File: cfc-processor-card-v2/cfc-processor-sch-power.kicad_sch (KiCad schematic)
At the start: 89 parts, among them Q1 DMP2240UDM, Q2 PMV45EN, Q3 DMP3050LVT-7, Q4 DMP3050LVT-7, Q5 PMV45EN, U1 MAX7310ATE+, U2 MIC842LYC5, U3 MIC842LYC5, U4 TS5A21366, U5 MAX4211FETE, U6 TPS62112

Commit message: Update
Updated OPD to align with proto card. Made changes from DR with Greenberg. Moved around polygon pours, led indicators, silkscreen issue date, etc. Ready for fab.
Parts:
- removed TP16, TP17, TP19: TEST-POINT, oresat-misc:TestPoint-0.75mm-th, symbol oresat-misc:Test-Point-0.75mm-th
- Q2, Q5: value PMV45EN -> DMN2050LQ-7; DPN 1727-2307-1-ND -> 31-DMN2050LQ-7CT-ND; MFR Nexperia -> Diodes Incorporated; MPN PMV45EN2R -> DMN2050LQ-7
- Q3, Q4: value DMP3050LVT-7 -> DMPH2040UVTQ-7; DPN DMP3050LVT-7DICT-ND -> 31-DMPH2040UVTQ-7CT-ND; MFR Diodes Inc -> Diodes Incorporated; MPN DMP3050LVT-7 -> DMPH2040UVTQ-7
- R1: value 10 -> 100; DPN RMCF0603FT10R0CT-ND -> RMCF0603FT100RCT-ND; MPN RMCF0603FT10R0 -> RMCF0603FT100R
- R11, R13, R3: value 100 -> 1k; DIS DigiKey -> Digi-Key; DPN RMCF0603FT100RCT-ND -> 1276-4275-1-ND; MFR Stackpole Electronics Inc -> Samsung; MPN RMCF0603FT100R -> RC1005F6653CS
- R24: value 10k -> 1k; DIS DigiKey -> Digi-Key; DPN RMCF0603FT10K0CT-ND -> 1276-4275-1-ND; MFR Stackpole Electronics Inc -> Samsung; MPN RMCF0603FT10K0 -> RC1005F6653CS
- R28: value 2.7k -> 4.7k; DPN RMCF0603FT2K70CT-ND -> RMCF0603FT4K70CT-ND; MPN RMCF0603FT2K70 -> RMCF0603FT4K70
- R39, R41: value 2.7k -> 10k; DPN RMCF0603FT2K70CT-ND -> RMCF0603FT10K0CT-ND; MPN RMCF0603FT2K70 -> RMCF0603FT10K0

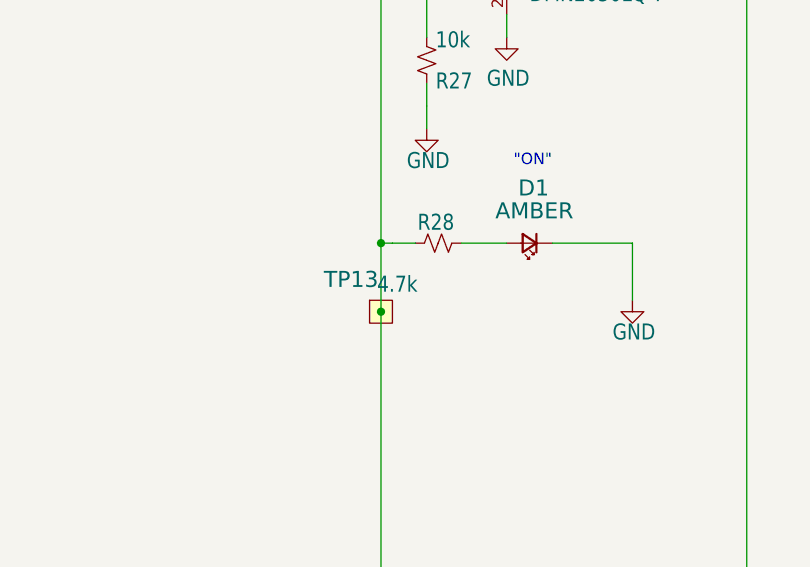
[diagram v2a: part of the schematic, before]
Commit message: Updated OPD on sensor card
updated OPD on sensor card to match protocard. Finished placement on PCB.
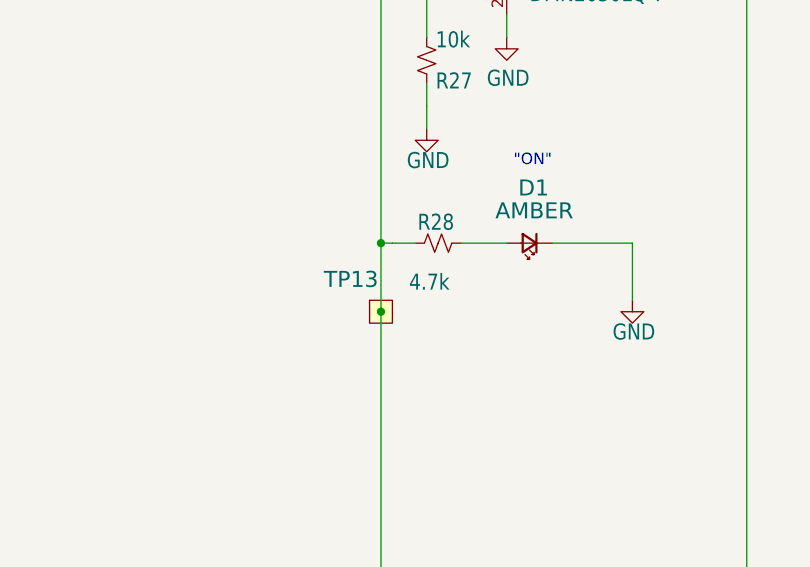
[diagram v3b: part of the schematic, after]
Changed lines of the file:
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@@
 		)
 		(property "Value" "4.7k"
-			(at 209.804 89.8906 90)
+			(at 213.36 89.662 90)
 			(show_name no)
 			(do_not_autoplace no)

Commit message: Update
Updated BOM, couple of fixes on OPD. Minor routing and layout changes. Removed logic gates from sensor card.
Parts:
- C1, C2, C6, C7, C9: DIS DigiKey -> Digikey; DPN 587-3473-1-ND -> 490-10675-2-ND; MFR Taiyo Yuden -> Murata Electronics; MPN TMK107BJ105KAHT -> GCM21BR71H105KA03L
- C10: DPN 490-GCM32EC71E226KE36KCT-ND -> 587-5949-1-ND; MFR Murata Electronics -> Taiyo Yuden; MPN GCM32EC71E226KE36K -> TMK325B7226KMHP
- C3, C4: DPN 587-3472-1-ND -> 399-6856-1-ND; MFR Taiyo Yuden -> KEMET; MPN TMK107BJ104KAHT -> C0603C104K5RACAUTO
- C5, C8: DPN 490-GRT21BC71E106KE13LCT-ND -> 490-GRT21BC71E106KE13KCT-ND; MPN GRT21BC71E106KE13L -> GRT21BC71E106KE13K
- D1, D2, D3: symbol Device:LED_Small -> Device:LED_Small_Filled
- Q1: value DMP2240UDM -> DMP2110UVTQ-7; DPN DMP2240UDMDICT-ND -> 31-DMP2110UVTQ-7CT-ND; MFR Diodes Inc -> Diodes Incorporated; MPN DMP2240UDM -> DMP2110UVTQ-7
- R10, R11, R12, R13, R16, R17, R2, R3, R4, R5, R8, R9: value 1k -> 100; DIS Digi-Key -> DigiKey; DPN 1276-4275-1-ND -> RMCF0603FT100RCT-ND; MFR Samsung -> Stackpole Electronics Inc; MPN RC1005F6653CS -> RMCF0603FT100R
- R24: DIS Digi-Key -> DigiKey; DPN 1276-4275-1-ND -> RMCF0603FT1K00CT-ND; MFR Samsung -> Stackpole Electronics Inc; MPN RC1005F6653CS -> RMCF0603FT1K00
- R63: MFR Stackpole Electronics -> Stackpole Electronics Inc
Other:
- moved on the sheet: C53
